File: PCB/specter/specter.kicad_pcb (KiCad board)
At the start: 2 copper layers, 120 parts, among them J1 USB_C_Receptacle_USB2.0_16P, J10 Conn_01x01, J11 Conn_01x01, J13 Conn_01x01, J14 Conn_01x01, J16 Conn_01x01, J17 Conn_01x01, J18 Conn_01x01, J19 Conn_01x01, J2 Micro_SD_Card_Det2, J22 SM04B-SRSS-TB_LF__SN_, J23 Conn_01x01, J24 SM04B-SRSS-TB_LF__SN_, J25 SM04B-SRSS-TB_LF__SN_, J26 SM04B-SRSS-TB_LF__SN_, J27 SM06B-SRSS-TB_LF__SN_, J28 SM06B-SRSS-TB_LF__SN_, J29 SM06B-SRSS-TB_LF__SN_, J30 SM06B-SRSS-TB_LF__SN_, J4 Conn_01x22_Socket, J5 Conn_01x22_Socket, J6 Conn_02x01, J7 Conn_01x03, J8 Conn_01x01, J9 Conn_02x01, U1 FT232RL, U2 FT232RL, U3 RT9742GGJ5, U4 MagJack-A70-112-331N126, U5 TPD4EUSB30, U6 TPD4EUSB30, U7 74LVC1G07_copy, U8 AP2553W6

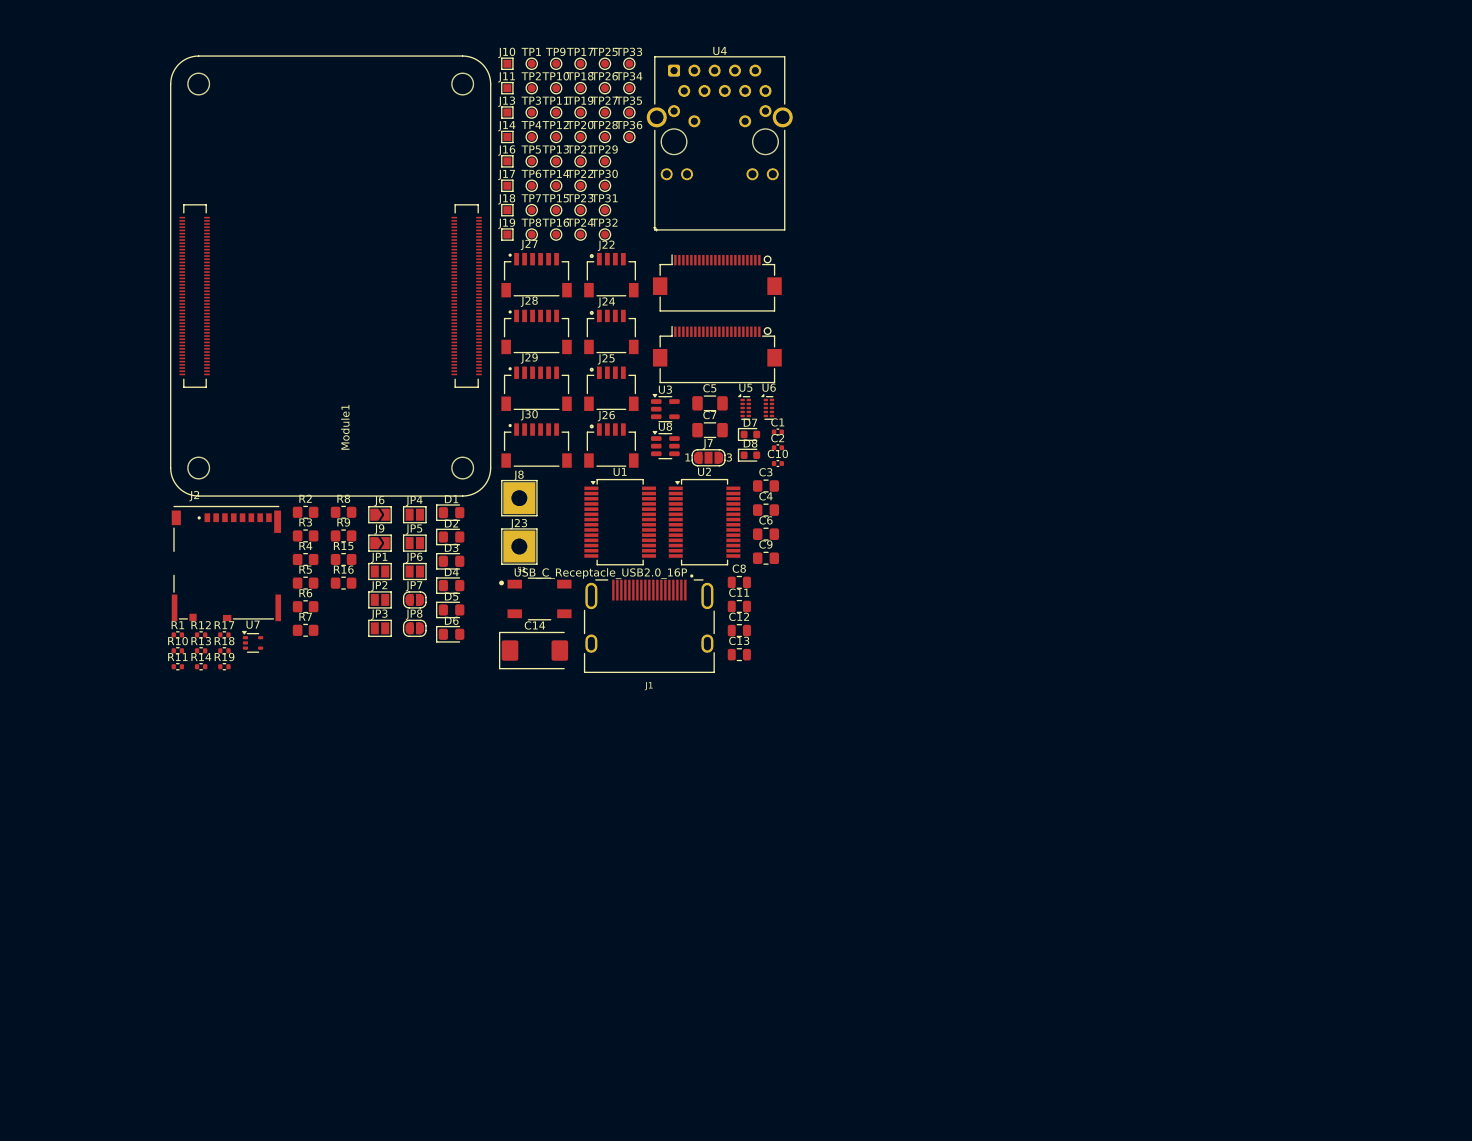
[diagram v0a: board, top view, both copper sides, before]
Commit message: added PCIe slot
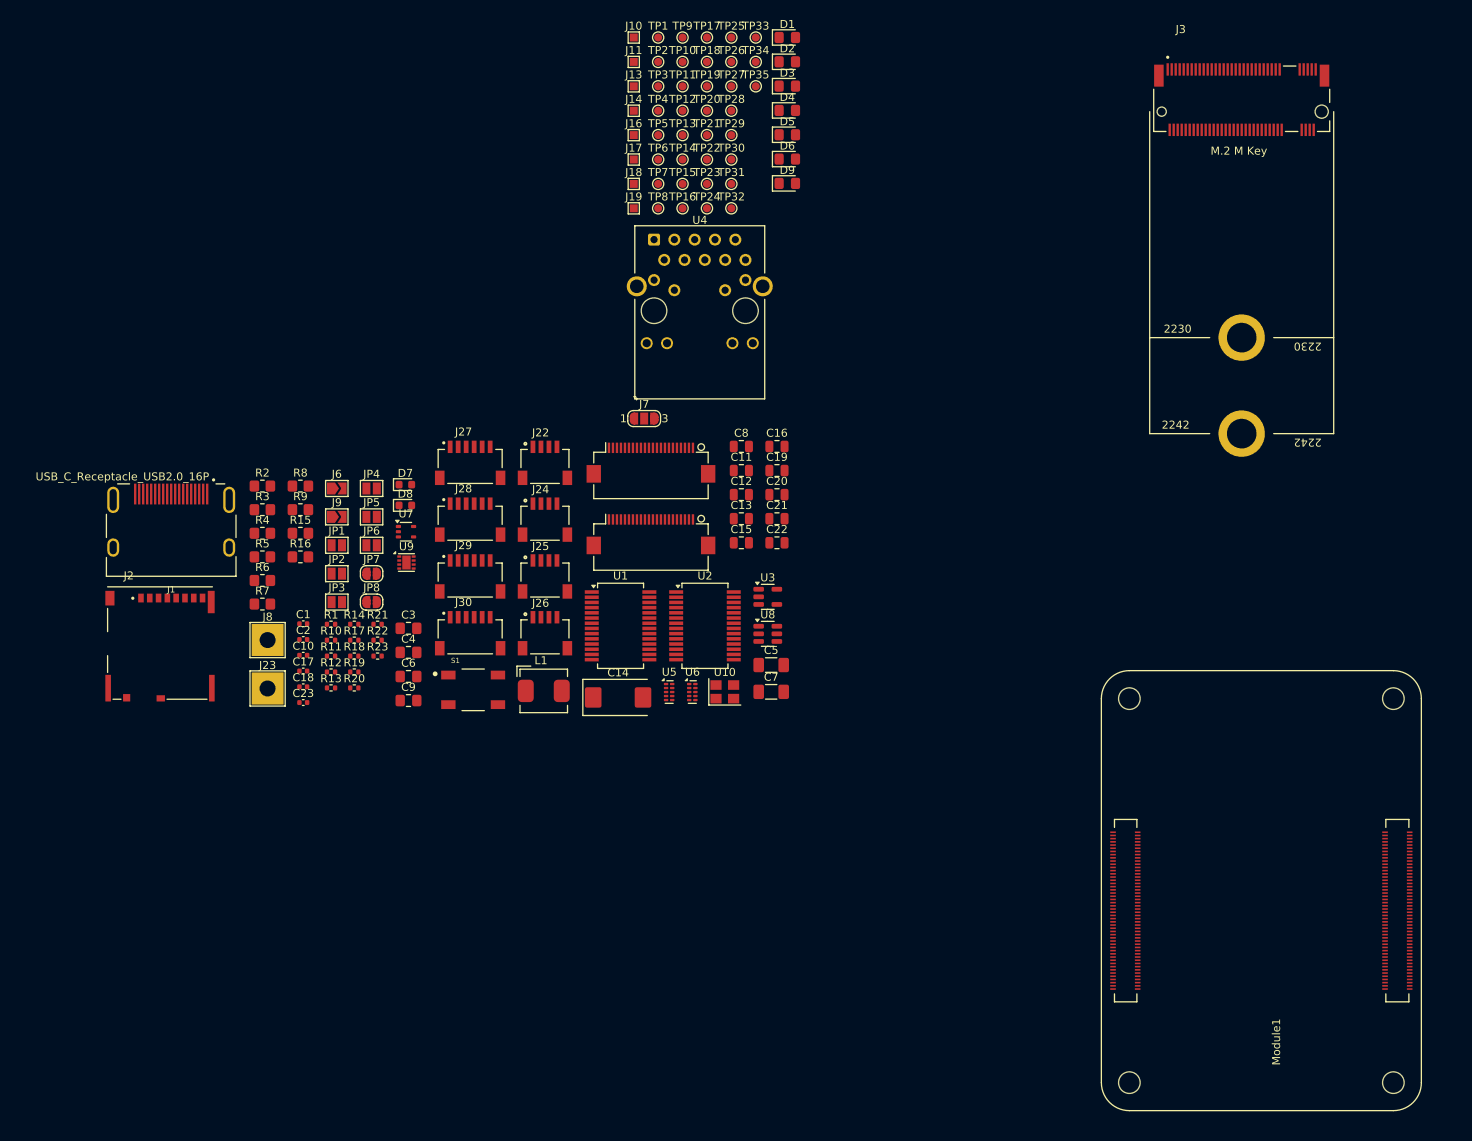
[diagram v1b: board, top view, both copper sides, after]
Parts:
- removed TP36: TestPoint, TestPoint:TestPoint_Pad_D1.0mm
- added C15: 10uF, Capacitor_SMD:C_0805_2012Metric, F.Cu at (96.8, 79.5)
- added C16: 10uF, Capacitor_SMD:C_0805_2012Metric, F.Cu at (101.2, 67.5)
- added C17: 100nF, Capacitor_SMD:C_0402_1005Metric, F.Cu at (42.0, 95.5)
- added C18: 4.7nF, Capacitor_SMD:C_0402_1005Metric, F.Cu at (42.0, 97.5)
- added C19: 10uF, Capacitor_SMD:C_0805_2012Metric, F.Cu at (101.2, 70.5)
- added C20: 10uF, Capacitor_SMD:C_0805_2012Metric, F.Cu at (101.2, 73.5)
- added C21: 10uF, Capacitor_SMD:C_0805_2012Metric, F.Cu at (101.2, 76.5)
- added C22: 10uF, Capacitor_SMD:C_0805_2012Metric, F.Cu at (101.2, 79.5)
- added C23: 100nF, Capacitor_SMD:C_0402_1005Metric, F.Cu at (42.0, 99.5)
- added D9: LED, LED_SMD:LED_0805_2012Metric_Pad1.15x1.40mm_HandSolder, F.Cu at (102.5, 34.6)
- added J3: Bus_M.2_Socket_M, CM5IO:M.2 M Key socket, F.Cu at (159.3, 25.6)
- added L1: 2.2uH, CM5IO:L_Bourns_SRP5030CC, F.Cu at (72.0, 98.0)
- added R20: 100K | 1%, Resistor_SMD:R_0402_1005Metric, F.Cu at (48.4, 97.7)
- added R21: 10K | 1%, Resistor_SMD:R_0402_1005Metric, F.Cu at (51.3, 89.7)
- added R22: 2.2K | 1%, Resistor_SMD:R_0402_1005Metric, F.Cu at (51.3, 91.7)
- added R23: 1K, Resistor_SMD:R_0402_1005Metric, F.Cu at (51.3, 93.7)
- added U10: ASEK-32.768KHZ-L-R-T, Crystal:Crystal_SMD_3225-4Pin_3.2x2.5mm, F.Cu at (94.7, 98.2)
- added U9: AP3441SHE-7B, Package_DFN_QFN:DFN-8-1EP_2x2mm_P0.5mm_EP1.05x1.75mm, F.Cu at (54.9, 82.0)
- C10: value 1nF -> 100nF
- R17: value 1k -> 1K
- moved Module1 139.4 mm to (145.2, 147.0)
- moved D2 72.7 mm to (102.5, 19.4)
- moved D5 72.7 mm to (102.5, 28.5)
- moved D1 72.7 mm to (102.5, 16.4)
- moved D3 72.7 mm to (102.5, 22.4)
- moved D4 72.7 mm to (102.5, 25.5)
- moved D6 72.7 mm to (102.5, 31.6)
- moved C1 64.0 mm to (42.0, 89.6)
- moved C10 64.0 mm to (42.0, 93.6)
- moved C2 64.0 mm to (42.0, 91.6)
- moved J1 61.0 mm to (25.5, 74.2)
- moved C3 48.1 mm to (55.1, 90.2)
- moved C4 48.1 mm to (55.1, 93.2)
- moved C6 48.1 mm to (55.1, 96.2)
- moved C9 48.1 mm to (55.1, 99.2)
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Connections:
- JP7 pad 2: /SCL0 -> /GPIO2
- JP8 pad 2: /GPIO3 -> /SDA1
- Module1 pad 102: unconnected-(Module1B-PCIe_nCLKREQ-Pad102) -> /PCIE_nCLKREQ
- Module1 pad 104: unconnected-(Module1B-PCIE_nWAKE-Pad104) -> /PCIE_nWAKE
- Module1 pad 106: unconnected-(Module1B-PCIE_PWR_EN-Pad106) -> /PCIE_PWR_EN
- Module1 pad 109: unconnected-(Module1B-PCIe_nRST-Pad109) -> /PCIE_nRST
- Module1 pad 110: unconnected-(Module1B-PCIe_CLK_P-Pad110) -> /PCIE_CLK_P
- Module1 pad 112: unconnected-(Module1B-PCIe_CLK_N-Pad112) -> /PCIE_CLK_N
- Module1 pad 116: unconnected-(Module1B-PCIe_RX_P-Pad116) -> /PCIE_RX_P
- Module1 pad 118: unconnected-(Module1B-PCIe_RX_N-Pad118) -> /PCIE_RX_N
- Module1 pad 122: unconnected-(Module1B-PCIe_TX_P-Pad122) -> /PCIE_TX_P
- Module1 pad 124: unconnected-(Module1B-PCIe_TX_N-Pad124) -> /PCIE_TX_N
- R13 pad 1: /GPIO3 -> /SDA1
- R14 pad 2: /SCL0 -> /GPIO2

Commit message: started PCB layout
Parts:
- added J13: Conn_01x01, TestPoint:TestPoint_Pad_1.0x1.0mm, B.Cu at (110.0, 86.5)
- added J13: Conn_01x01, TestPoint:TestPoint_Pad_1.0x1.0mm, B.Cu at (110.0, 75.2)
- added J13: Conn_01x01, TestPoint:TestPoint_Pad_1.0x1.0mm, B.Cu at (110.0, 72.8)
- added J13: Conn_01x01, TestPoint:TestPoint_Pad_1.0x1.0mm, B.Cu at (110.0, 84.0)
- C15, C16, C17, C18, C19, C20, C21, C22, C23, C3, C4, C5, C6, C7, C8, C9, D9, J10, J11, J13, J14, J16, J17, J18, J19, J2, J3, JP1, JP2, JP3, JP4, JP5, JP6, L1, R2, R20, R21, R22, R23, R3, R4, R5, R6, R7, R8, R9, TP1, TP10, TP11, TP12, TP13, TP14, TP15, TP16, TP17, TP18, TP19, TP2, TP20, TP21, TP22, TP23, TP24, TP25, TP26, TP27, TP28, TP29, TP3, TP30, TP31, TP32, TP34, TP4, TP5, TP6, TP7, TP8, TP9, U1, U10, U2, U3, U9: moved to B.Cu
- J1: footprint CM5IO:EDAC 690-019-298-412 -> Connector_USB:USB_C_Receptacle_GCT_USB4105-xx-A_16P_TopMnt_Horizontal
- moved TP9 159.7 mm to (178.9, 148.6), turned to 90 degrees
- moved TP25 159.5 mm to (185.6, 148.0), turned to 90 degrees
- moved TP10 154.0 mm to (172.4, 149.2), turned to 90 degrees
- moved TP17 153.0 mm to (178.9, 142.7), turned to 90 degrees
- moved TP11 148.0 mm to (168.1, 147.8), turned to 90 degrees
- moved TP18 147.3 mm to (172.4, 143.2), turned to 90 degrees
- moved TP26 143.1 mm to (172.4, 140.2), turned to 90 degrees
- moved TP12 142.8 mm to (163.1, 147.8), turned to 90 degrees
- moved TP19 141.4 mm to (168.1, 141.9), turned to 90 degrees
- moved TP34 138.9 mm to (172.4, 137.1), turned to 90 degrees
- moved TP13 137.8 mm to (158.4, 147.8), turned to 90 degrees
- moved TP27 137.2 mm to (168.1, 138.8), turned to 90 degrees
- moved TP20 136.2 mm to (163.1, 141.9), turned to 90 degrees
- moved R5 133.2 mm to (169.3, 94.8), turned to 90 degrees
- moved TP14 132.3 mm to (153.1, 147.6), turned to 90 degrees
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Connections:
- net /RX1 renamed /RX_TELEM
- net /RX2 renamed /RX_CRSF
- net /TX1 renamed /TX_TELEM
- net /TX2 renamed /TX_CRSF
- J4 pad 21: /GPIO3 -> /SDA0
- J5 pad 20: /GPIO2 -> /SCL1
- JP7 pad 2: /GPIO2 -> /SCL1
- Module1 pad 82: /GPIO3 -> /SDA0
- R14 pad 2: /GPIO2 -> /SCL1
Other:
- copper layers 2 -> 4

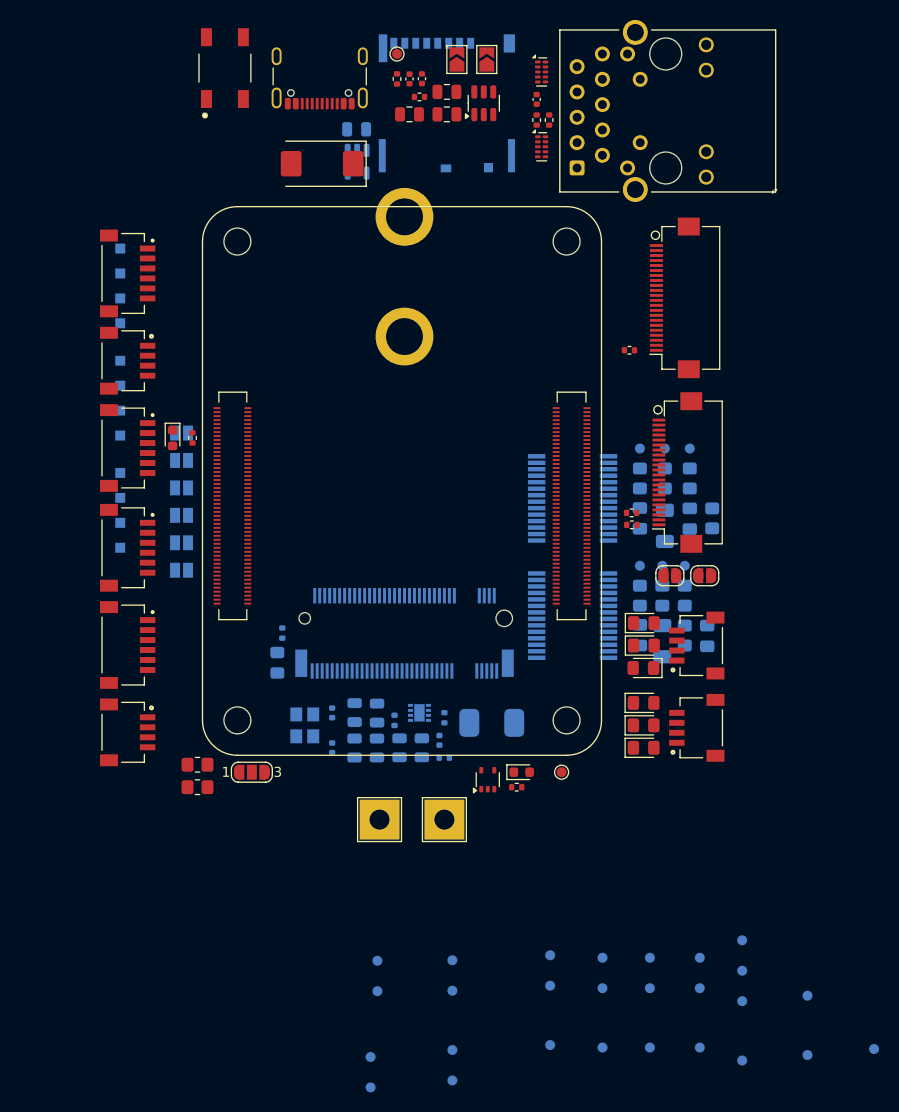
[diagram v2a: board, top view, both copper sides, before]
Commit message: updated PCB layout
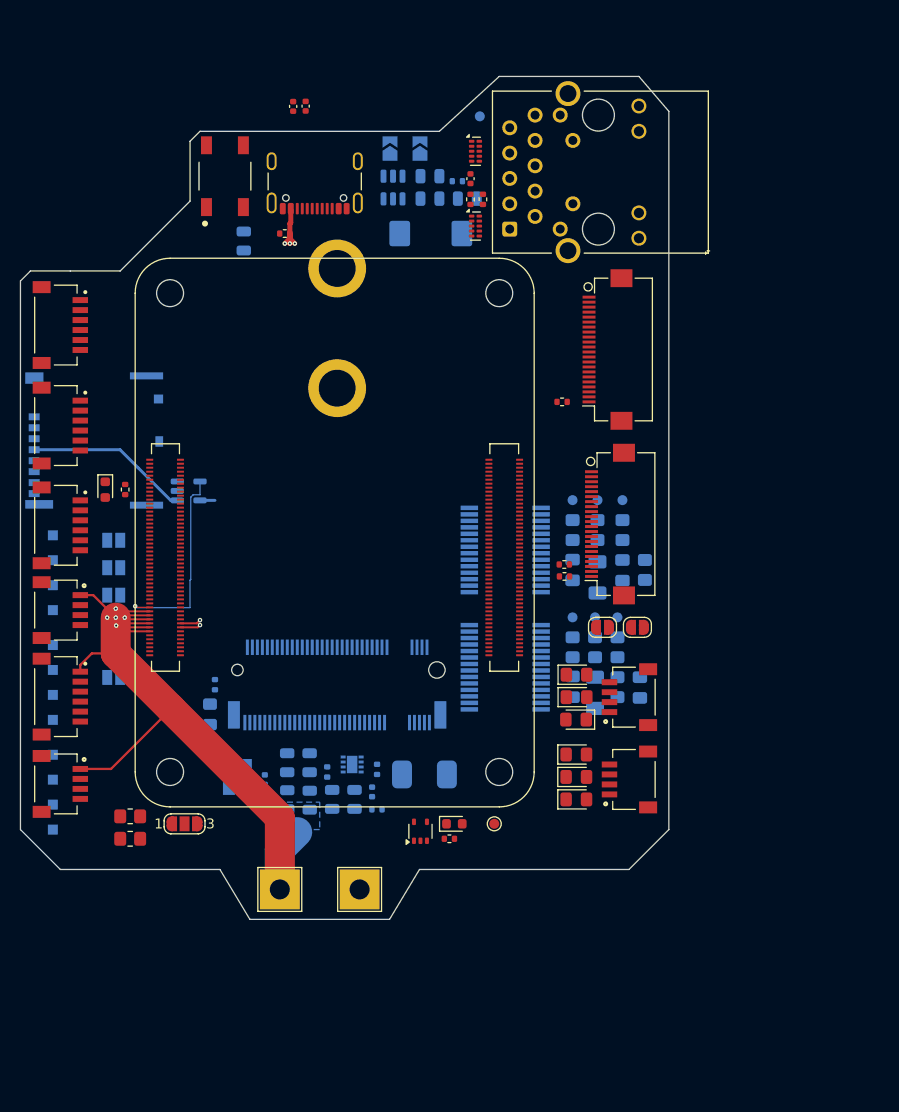
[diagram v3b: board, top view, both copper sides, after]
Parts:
- removed TP10, TP11, TP12, TP13, TP14, TP15, TP16, TP17, TP18, TP19, TP20, TP21, TP22, TP23, TP24, TP25, TP26, TP27, TP28, TP29, TP30, TP31, TP32, TP34, TP7, TP8, TP9: TestPoint, TestPoint:TestPoint_Pad_D1.0mm
- C11, C12, C13, C14, J6, J9, R18, TP35, U8: moved to B.Cu
- moved J2 49.5 mm to (107.0, 87.0), turned to -90 degrees
- moved U3 37.1 mm to (116.9, 92.0), turned to 0 degrees
- moved J13 29.5 mm to (103.2, 104.0)
- moved J13 29.5 mm to (103.2, 101.5)
- moved J13 29.5 mm to (103.2, 99.0)
- moved J14 29.5 mm to (103.2, 96.5)
- moved J10 29.3 mm to (103.2, 110.0)
- moved J11 29.3 mm to (103.2, 107.5)
- moved J13 29.3 mm to (103.2, 115.0)
- moved J13 29.3 mm to (103.2, 112.5)
- moved J16 29.0 mm to (103.2, 126.0)
- moved J17 29.0 mm to (103.2, 118.5)
- moved J18 29.0 mm to (103.2, 121.0)
- moved J19 29.0 mm to (103.2, 123.5)
- moved J22 25.9 mm to (106.0, 104.0)
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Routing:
- net /+5v: track 0.00 -> 91.6 mm, vias 0 -> 8
- net /SD_PWR_ON: track 0.00 -> 20.5 mm, vias 0 -> 1
- net /SD_PWR: track 0.00 -> 16.5 mm
- net /+3.3v: track 0.00 -> 5.65 mm, vias 0 -> 2
- added copper zone on B.Cu, net /+5v
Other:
- board outline added: 65 x 84.5 mm

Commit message: started PCB traces
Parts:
- moved C17 54.3 mm to (138.2, 71.0), turned to -90 degrees
- moved R22 54.2 mm to (127.0, 70.5), turned to 0 degrees
- moved C15 52.4 mm to (136.0, 71.5), turned to -90 degrees
- moved C16 51.9 mm to (133.8, 71.4), turned to -90 degrees
- moved C20 51.6 mm to (129.3, 71.5), turned to 90 degrees
- moved C19 51.5 mm to (131.5, 71.5), turned to 90 degrees
- moved U10 50.8 mm to (141.0, 73.8), turned to -90 degrees
- moved C18 50.6 mm to (127.5, 72.2), turned to -90 degrees
- moved L1 49.9 mm to (122.2, 74.0), turned to 180 degrees
- moved C23 49.5 mm to (138.2, 73.5), turned to 90 degrees
- moved R20 46.3 mm to (127.0, 74.5), turned to 90 degrees
- moved R21 46.0 mm to (132.0, 74.2), turned to -90 degrees
- moved C21 45.1 mm to (136.0, 75.2), turned to 90 degrees
- moved U9 44.6 mm to (129.5, 75.0), turned to 180 degrees
- moved C22 44.4 mm to (133.8, 75.2), turned to 90 degrees
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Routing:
- net /PCIE_RX_N: track 0.00 -> 48.6 mm, vias 0 -> 1
- net /PCIE_RX_P: track 0.00 -> 48.5 mm, vias 0 -> 1
- net /PCIE_TX_N: track 0.00 -> 46.0 mm, vias 0 -> 1
- net /PCIE_TX_P: track 0.00 -> 46.0 mm, vias 0 -> 1
- net /PCIE_CLK_N: track 0.00 -> 34.1 mm, vias 0 -> 1
- net /PCIE_CLK_P: track 0.00 -> 34.0 mm, vias 0 -> 1
- net /DPHY0_D0_N: track 0.00 -> 33.5 mm, vias 0 -> 2
- net /DPHY0_D0_P: track 0.00 -> 33.5 mm, vias 0 -> 2
- net /DPHY0_D2_N: track 0.00 -> 33.4 mm, vias 0 -> 2
- net /DPHY0_D2_P: track 0.00 -> 33.4 mm, vias 0 -> 2
- net /DPHY0_D3_P: track 0.00 -> 33.3 mm, vias 0 -> 2
- net /DPHY0_D3_N: track 0.00 -> 33.1 mm, vias 0 -> 2
- net /DPHY0_D1_P: track 0.00 -> 33.1 mm, vias 0 -> 2
- net /DPHY0_D1_N: track 0.00 -> 33.0 mm, vias 0 -> 2
- net /DPHY_C_P: track 0.00 -> 32.5 mm, vias 0 -> 2
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- removed copper zone on B.Cu, net /+5v
